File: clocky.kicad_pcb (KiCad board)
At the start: 4 copper layers, 79.9 x 38 mm, 73 parts, among them J1 Bot 50 pin, J2 Bot 40 pin, J3 Top 50 pin, J4 Top 40 pin, J5 Power, J6 JST_PH, J8 Program, Q1 AO3401A, U1 HEF4094B, U10 TMP117xxDRV, U2 HEF4094B, U3 HEF4094B, U4 HEF4094B, U5 HEF4094B, U6 HEF4094B, U7 TPS63060, U8 TPS7A0233PDBV, U9 STM32U031C8Ux, Y1 32768Hz

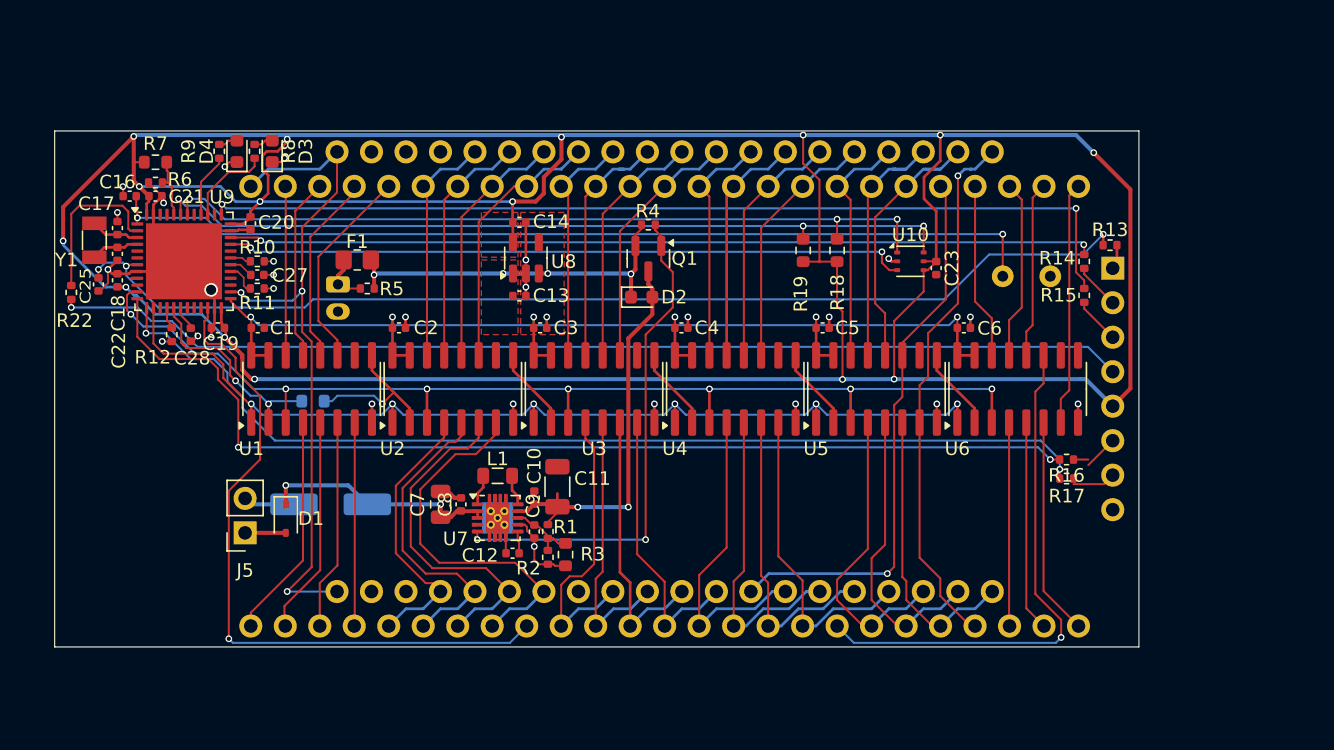
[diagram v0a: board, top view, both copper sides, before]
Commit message: DRC passes.
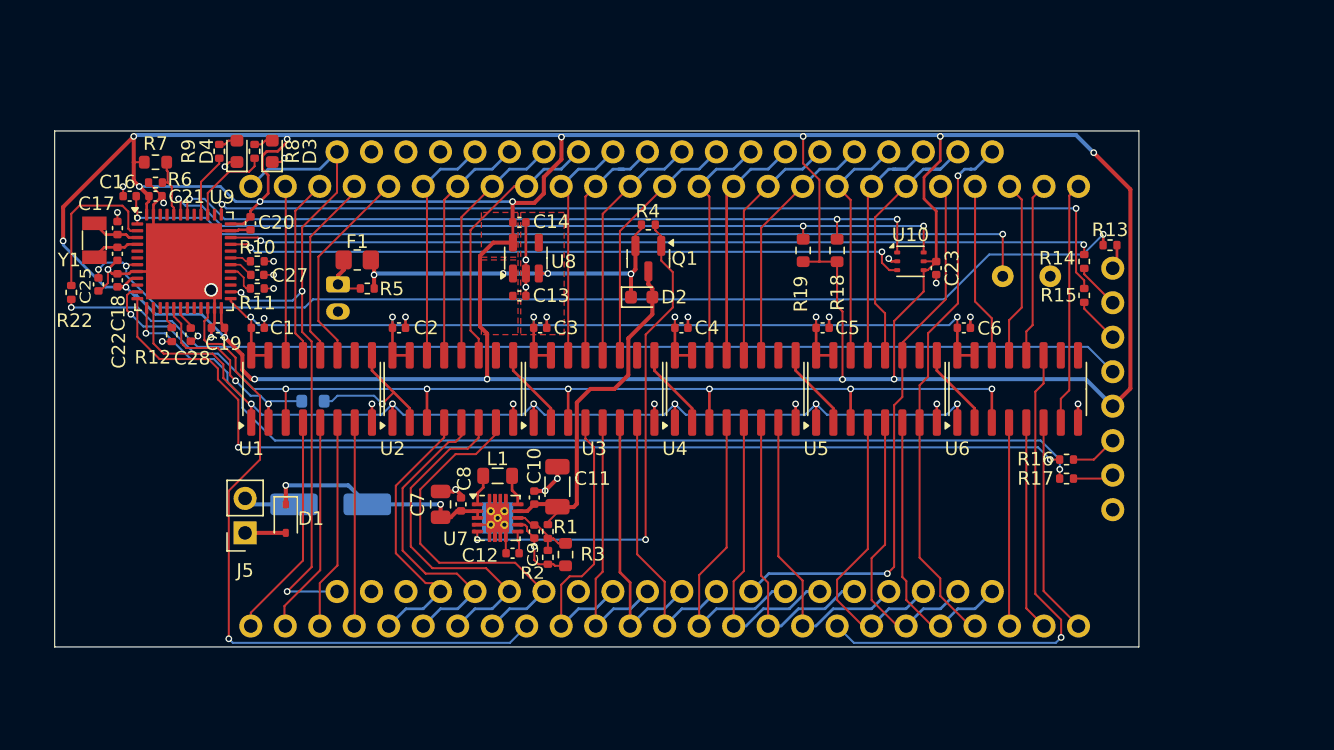
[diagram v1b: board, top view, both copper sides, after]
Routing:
- net +3V3: track 285.6 -> 298.4 mm, vias 15 -> 16
- net GND: track 53.8 -> 58.2 mm, vias 25 -> 30
- net /VBatt: track 29.2 -> 26.0 mm, vias 2 -> 0
- net /Q4D: track 17.5 -> 16.8 mm
- net Net-(U7-FB): track 5.01 -> 4.44 mm
- net /Q2P: track 19.3 -> 19.8 mm
- net /Q2B: track 27.2 -> 26.7 mm

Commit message: Sort the touch pads out a bit.
Zones still need work.
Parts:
- added TP1: TestPoint, Parts:Dummy, F.Cu at (121.2, 90.6)
- added TP2: TestPoint, Parts:Dummy, F.Cu at (121.2, 92.6)
- added TP3: TestPoint, Parts:Dummy, F.Cu at (113.0, 96.5)
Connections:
- R10 pad 1: unconnected-(R10-Pad1) -> /PlusPad
- R11 pad 1: unconnected-(R11-Pad1) -> /MinusPad
- R12 pad 1: unconnected-(R12-Pad1) -> /ExtraPad
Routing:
- net GND: track 58.2 -> 101.6 mm, vias 30 -> 34
- net unconnected-(R11-Pad1): track 27.2 -> 0.00 mm, vias 1 -> 0
- net /MinusPad: track 0.00 -> 27.2 mm, vias 0 -> 1
- net unconnected-(R10-Pad1): track 17.9 -> 0.00 mm, vias 1 -> 0
- net /PlusPad: track 0.00 -> 17.6 mm, vias 0 -> 1
- net unconnected-(R12-Pad1): track 3.40 -> 0.00 mm, vias 1 -> 0
- net /ExtraPad: track 0.00 -> 3.40 mm, vias 0 -> 1

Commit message: Do a round of tidy-up on clocky.
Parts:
- removed R5: 470, Resistor_SMD:R_0402_1005Metric
- added D5: 1N5819WS, Diode_SMD:D_SOD-323, F.Cu at (129.2, 92.4)
- R20: moved to F.Cu
- moved F1 1.85 mm to (129.2, 90.3)
- moved C24 1.00 mm to (126.4, 108.5)
- moved R20 0.91 mm to (124.0, 100.0)
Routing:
- net GND: track 101.6 -> 92.6 mm, vias 34 -> 32
- net +3V3: track 298.4 -> 293.6 mm
- net Net-(D5-A): track 3.32 -> 5.46 mm
- net /Q2F: track 22.5 -> 20.6 mm
- net /Q2A: track 25.0 -> 23.4 mm
- net /Vin: track 17.7 -> 16.3 mm
- net /Q2B: track 26.7 -> 25.4 mm
- net +BATT: track 27.2 -> 25.8 mm
- net /CP: track 82.9 -> 83.9 mm
- net /DAT: track 15.6 -> 16.5 mm
- net /Q3G: track 21.6 -> 20.8 mm
- net /Q2G: track 20.2 -> 19.3 mm
- net /PlusPad: track 17.6 -> 18.4 mm
- net /MinusPad: track 27.2 -> 26.5 mm
- net /SERRX: track 75.3 -> 75.9 mm, vias 2 -> 3
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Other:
- board text added: "3V7"
- board text added: "GND"
- board text added: "Vin"
- board text added: "≡"

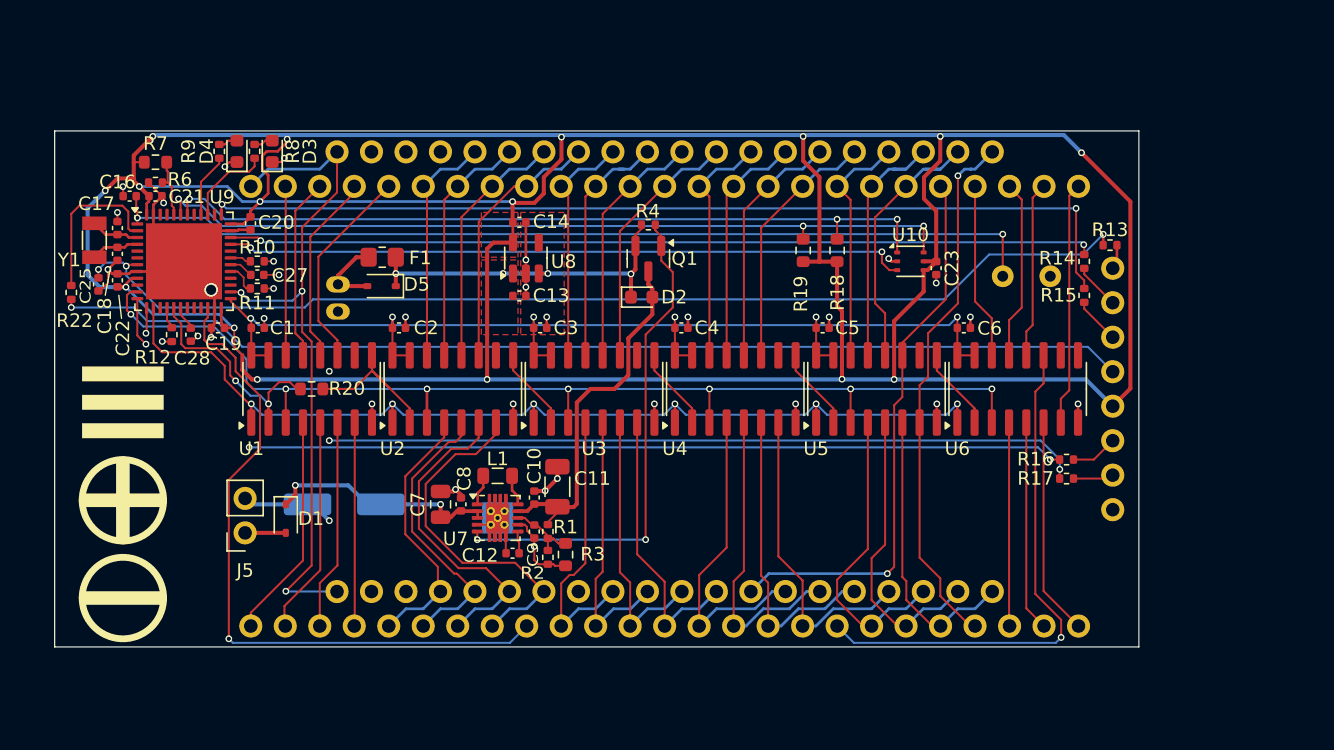
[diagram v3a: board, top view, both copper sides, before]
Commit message: Rotate CPU on clocky.  Tidy up every where.
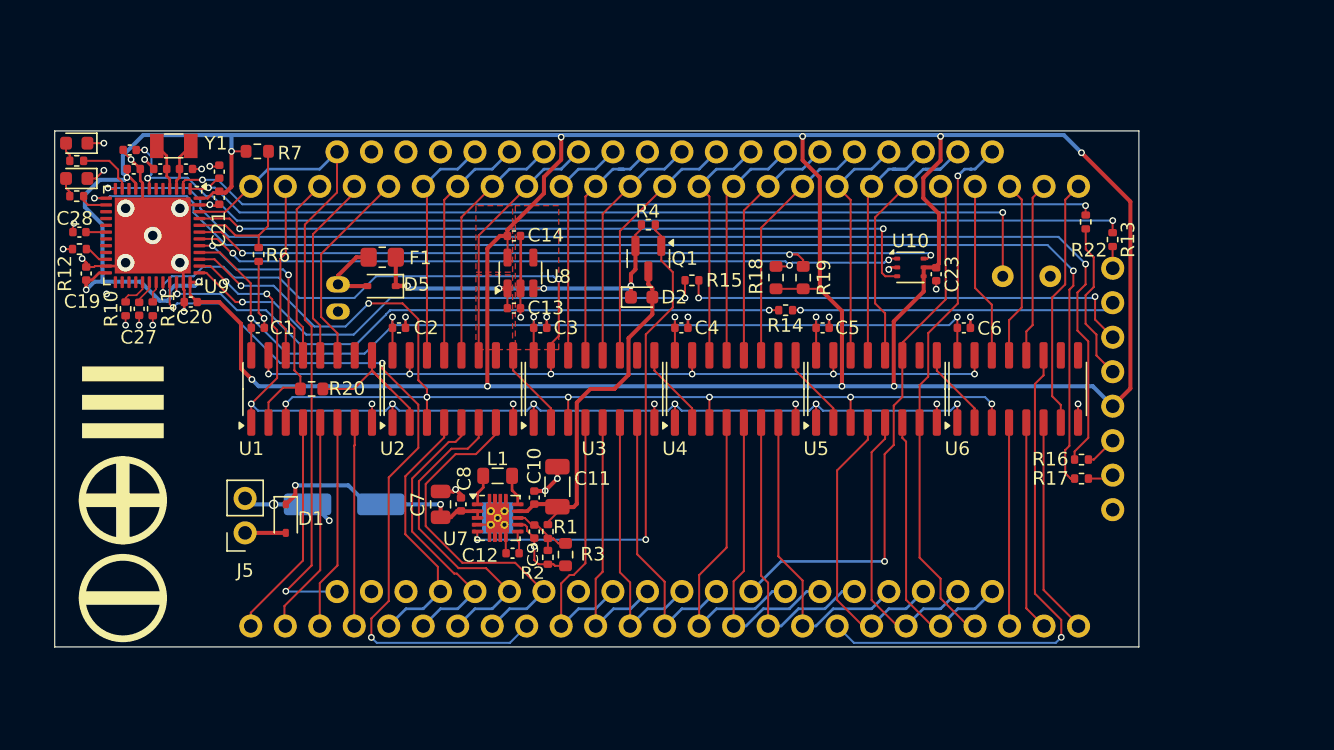
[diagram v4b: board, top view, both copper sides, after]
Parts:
- moved R22 74.9 mm to (181.0, 87.7)
- moved R15 28.9 mm to (152.0, 92.0), turned to 180 degrees
- moved R14 22.3 mm to (158.9, 94.2), turned to 180 degrees
- moved D3 14.4 mm to (106.7, 81.9), turned to 180 degrees
- moved R8 13.1 mm to (106.7, 83.2), turned to 180 degrees
- moved D4 12.0 mm to (106.7, 84.5), turned to 180 degrees
- moved TP1 11.9 mm to (110.3, 95.3), turned to -90 degrees
- moved C28 11.1 mm to (106.9, 88.5), turned to 180 degrees
- moved R9 11.0 mm to (106.7, 85.8), turned to 180 degrees
- moved C19 10.5 mm to (107.4, 91.5), turned to 90 degrees
- moved R10 10.3 mm to (110.3, 94.1), turned to 90 degrees
- moved C25 10.2 mm to (110.6, 82.4), turned to 180 degrees
- moved TP3 9.98 mm to (105.7, 89.7), turned to -90 degrees
- moved TP2 9.30 mm to (112.3, 95.3), turned to -90 degrees
- moved R12 9.27 mm to (106.9, 89.7), turned to 0 degrees
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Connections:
- U1 pad 15: /DPWR -> /OE
- U2 pad 15: /DPWR -> /OE
- U3 pad 15: /DPWR -> /OE
- U4 pad 15: /DPWR -> /OE
- U5 pad 15: /DPWR -> /OE
- U6 pad 15: /DPWR -> /OE
- U9 pad 11: /CP -> /Green
- U9 pad 14: /STR -> /Red
- U9 pad 16: /Extra -> unconnected-(U9-PA6-Pad16)
- U9 pad 17: /DAT -> unconnected-(U9-PA7-Pad17)
- U9 pad 22: /COL1 -> /Extra
- U9 pad 25: /DPWR -> unconnected-(U9-PB12-Pad25)
- U9 pad 26: /COM -> unconnected-(U9-PB13-Pad26)
- U9 pad 29: /Minus -> /Plus
- U9 pad 31: /Plus -> /Minus
- U9 pad 32: unconnected-(U9-PA11-Pad32) -> /OE
- U9 pad 33: /Alert -> /COL1
- U9 pad 38: unconnected-(U9-PA15-Pad38) -> /STR
- U9 pad 39: /Green -> /CP
- U9 pad 40: /Red -> /DPWR
- U9 pad 41: unconnected-(U9-PB5-Pad41) -> /DAT
- U9 pad 45: unconnected-(U9-PB8-Pad45) -> /Alert
- U9 pad 46: unconnected-(U9-PB9-Pad46) -> /COM
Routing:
- net /OE: track 0.00 -> 98.0 mm, vias 0 -> 8
- net /PRTC: track 79.3 -> 11.8 mm, vias 1 -> 0
- net /RTCOUT: track 11.9 -> 68.5 mm, vias 0 -> 2
- net /PSWC: track 3.44 -> 34.0 mm, vias 0 -> 2
- net /SWCLK: track 70.0 -> 40.1 mm
- net /PSWD: track 3.40 -> 23.8 mm, vias 0 -> 1
- net +3V3: track 293.6 -> 273.8 mm, vias 16 -> 12
- net GND: track 92.6 -> 73.0 mm, vias 32 -> 38
- net /SWDIO: track 63.8 -> 47.8 mm
- net /SERRX: track 75.9 -> 91.7 mm, vias 3 -> 2
- net /SERTX: track 76.9 -> 90.6 mm, vias 3 -> 2
- net /BOOT0: track 4.47 -> 12.0 mm
- net /ExtraPad: track 3.39 -> 10.4 mm
- net /Alert: track 50.3 -> 55.2 mm
- net /PlusPad: track 18.4 -> 23.1 mm
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
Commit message: Tweak power & zones.
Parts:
- added D6: 1N4148, Diode_SMD:D_0603_1608Metric, F.Cu at (178.1, 82.2)
- added R5: 100, Resistor_SMD:R_0603_1608Metric, F.Cu at (174.9, 89.0)
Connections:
- C15 pad 1: /VCap -> Net-(C15-Pad1)
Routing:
- net /ExtraPad: track 10.4 -> 15.9 mm
- net /VCap: track 66.2 -> 69.7 mm
- net /PlusPad: track 23.1 -> 21.1 mm
- net Net-(C15-Pad1): track 0.00 -> 1.83 mm
- net /MinusPad: track 30.4 -> 29.0 mm
- net +3V3: track 273.8 -> 274.6 mm
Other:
- board text added: "TODO - decide on main power connector."

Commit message: Final updates.  Ordered.
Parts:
- added R20: 10k, Resistor_SMD:R_0603_1608Metric, F.Cu at (168.1, 88.2)
- C9: footprint Capacitor_SMD:C_0402_1005Metric -> Capacitor_SMD:C_0603_1608Metric
- Q1: value AO3401A -> SI2301A
- U7: footprint Package_SON:Texas_S-PWSON-N10_ThermalVias -> Package_SON:Texas_S-PWSON-N10
- moved D1 6.29 mm to (128.3, 108.5)
- moved R3 3.20 mm to (144.7, 109.7), turned to 90 degrees
- moved R2 2.51 mm to (140.4, 110.1)
- moved C9 2.41 mm to (142.2, 112.1), turned to 0 degrees
- moved J5 1.60 mm to (120.7, 110.6)
- moved R1 0.66 mm to (141.9, 110.1), turned to 0 degrees
- moved R7 0.61 mm to (119.9, 81.9)
- moved R15 0.50 mm to (152.0, 92.5)
- renumbered R20 to R21
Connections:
- R10 pad 1: /PlusPad -> /MinusPad
- R10 pad 2: /Plus -> /Minus
- R11 pad 1: /MinusPad -> /PlusPad
- R11 pad 2: /Minus -> /Plus
- TP1 pad 1: /PlusPad -> /MinusPad
- TP2 pad 1: /MinusPad -> /PlusPad
- U9 pad 29: /Plus -> /Minus
- U9 pad 31: /Minus -> /Plus
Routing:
- net /PlusPad: track 21.1 -> 29.3 mm
- net /MinusPad: track 29.0 -> 21.0 mm
- net Net-(D1-A): track 3.00 -> 8.65 mm, vias 0 -> 1
- net GND: track 73.0 -> 67.9 mm, vias 38 -> 49
- net /Vin: track 16.3 -> 11.3 mm
- net Net-(U7-FB): track 4.44 -> 7.49 mm
- net /Q3G: track 20.8 -> 22.6 mm
- net +3V3: track 274.6 -> 275.9 mm
- net /Alert: track 55.2 -> 56.4 mm
- net /Q3F: track 20.1 -> 20.9 mm
- net /Plus: track 2.32 -> 1.56 mm
- net /Minus: track 1.56 -> 2.32 mm
- net /VBatt: track 26.0 -> 26.6 mm
- net /BOOT0: track 12.0 -> 12.6 mm
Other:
- board text removed: "TODO - decide on main power connector."

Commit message: Tweaks.  Fabbing.
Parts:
- removed the C12 at (138.8, 112.1)
- removed the C13 at (138.9, 94.0)
- removed C24: 220u, Capacitor_SMD:CP_Elec_6.3x7.7
- removed the C7 at (133.5, 108.5)
- removed D4: Red, LED_SMD:LED_0603_1608Metric
- removed D5: 1N5819WS, Diode_SMD:D_SOD-323
- removed F1: 116mA, Resistor_SMD:R_0805_2012Metric_Pad1.20x1.40mm_HandSolder
- removed Q1: SI2301A, Package_TO_SOT_SMD:SOT-23
- removed the R1 at (141.9, 110.1)
- removed the R3 at (144.7, 109.7)
- removed the R4 at (148.8, 87.9)
- removed the R9 at (106.7, 85.8)
- removed U8: TPS7A0233PDBV, Package_TO_SOT_SMD:SOT-23-5
- added C10: 100u, Capacitor_SMD:C_1206_3216Metric, F.Cu at (128.1, 90.2)
- added C23: 1u, Capacitor_SMD:C_0402_1005Metric, F.Cu at (151.7, 107.5)
- added L2: 22u, Inductor_SMD:L_0805_2012Metric_Pad1.05x1.20mm_HandSolder, F.Cu at (152.2, 106.0)
- added R18: 0R, Resistor_SMD:R_0603_1608Metric, F.Cu at (145.6, 112.9)
- added R19: 0R, Resistor_SMD:R_0603_1608Metric, F.Cu at (142.1, 112.9)
- added R21: 845k, Resistor_SMD:R_0603_1608Metric, F.Cu at (161.1, 110.5)
- added R22: 5M6, Resistor_SMD:R_0603_1608Metric, F.Cu at (157.9, 110.5)
- added R23: 3M3, Resistor_SMD:R_0603_1608Metric, F.Cu at (154.7, 110.5)
- added R24: 6M8, Resistor_SMD:R_0603_1608Metric, F.Cu at (161.1, 112.5)
- added R25: 150k, Resistor_SMD:R_0603_1608Metric, F.Cu at (157.9, 112.5)
- added R26: 2M7, Resistor_SMD:R_0603_1608Metric, F.Cu at (154.7, 112.5)
- added R28: 330k, Resistor_SMD:R_0603_1608Metric, F.Cu at (157.9, 108.5)
- added R29: 3M6, Resistor_SMD:R_0603_1608Metric, F.Cu at (154.7, 108.5)
- added TP4: TestPoint_Probe, Parts:TestPoint, F.Cu at (170.8, 106.3)
- added TP5: TestPoint_Probe, Parts:TestPoint, F.Cu at (147.9, 91.8)
- added TP6: TestPoint_Probe, Parts:TestPoint, F.Cu at (173.4, 106.3)
- added TP7: TestPoint_Probe, Parts:TestPoint, F.Cu at (139.1, 105.7)
- C11: footprint Capacitor_SMD:C_1206_3216Metric -> Capacitor_SMD:C_0805_2012Metric
- C12: renamed from C14; value 10u -> 10n
- C27, C28: value 22n -> 330p
- C7: renamed from C10; value 1u -> 10u; footprint Capacitor_SMD:C_0402_1005Metric -> Capacitor_SMD:C_0603_1608Metric
- C8: value 1u -> 10u; footprint Capacitor_SMD:C_0402_1005Metric -> Capacitor_SMD:C_0603_1608Metric
- C9: value 10p -> 10n; footprint Capacitor_SMD:C_0603_1608Metric -> Capacitor_SMD:C_0402_1005Metric
- D2: value 1N4148 -> 5V1; footprint Diode_SMD:D_0603_1608Metric -> Diode_SMD:D_SOD-323
- L1: value 1u -> 10u; footprint Inductor_SMD:L_0805_2012Metric -> Inductor_SMD:L_0805_2012Metric_Pad1.05x1.20mm_HandSolder
- R27: renamed from R2; value 150k -> 6M8; footprint Resistor_SMD:R_0402_1005Metric -> Resistor_SMD:R_0603_1608Metric
- R7: renamed from R10; value 10k -> 1k
- R8: renamed from R11; value 10k -> 1k
- R9: renamed from R12; value 10k -> 1k
- U7: value TPS63060 -> BQ25570; footprint Package_SON:Texas_S-PWSON-N10 -> Package_DFN_QFN:QFN-20-1EP_3.5x3.5mm_P0.5mm_EP2x2mm
- moved C12 23.2 mm to (146.0, 110.8), turned to 180 degrees
- moved R27 20.8 mm to (161.1, 108.5), turned to 180 degrees
- moved D2 16.3 mm to (142.7, 108.5), turned to -90 degrees
- moved C11 14.0 mm to (156.0, 106.0), turned to 0 degrees
- moved C8 13.6 mm to (148.3, 105.5), turned to 0 degrees
- moved D1 12.4 mm to (140.7, 108.5)
- moved U7 11.6 mm to (149.3, 110.1)
- moved C9 8.54 mm to (148.9, 106.8)
- moved L1 8.24 mm to (145.9, 107.2), turned to 0 degrees
- moved C7 5.07 mm to (145.4, 108.8), turned to 0 degrees
- renumbered C23 to C13, C25 to C14, R13 to R1, R5 to R10, R8 to R11, R21 to R12, R6 to R13, R18 to R14, R19 to R15, R20 to R16, R7 to R17, R14 to R2, R15 to R3, R22 to R4, R16 to R5, R17 to R6
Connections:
- net /Green renamed /White
- C11 pad 1: /VBatt -> +3V3
- C12 pad 1: +3V3 -> Net-(U7-VREF_SAMP)
- C7 pad 1: /VBatt -> /Vin
- C8 pad 1: /Vin -> GND
- C8 pad 2: GND -> /VStor
- C9 pad 2: Net-(U7-FB) -> /VStor
- D2 pad 1: +BATT -> /Vin
- D2 pad 2: /VBatt -> GND
- J6 pad 1: Net-(D5-A) -> GND
- J6 pad 2: GND -> /VBatt
- L1 pad 1: Net-(U7-L2) -> /Vin
- L1 pad 2: Net-(U7-L1) -> Net-(U7-LBOOST)
- R27 pad 1: Net-(U7-FB) -> /VRDIV
- R27 pad 2: GND -> /VOUT_SET
- U7 pad 1: Net-(U7-L1) -> GND
- U7 pad 10: Net-(U7-L2) -> /OK_HYST
- U7 pad 11: GND -> /OK_PROG
- U7 pad 3: /Vin -> /VStor
- U7 pad 4: GND -> Net-(U7-VREF_SAMP)
- U7 pad 5: /PGood -> GND
- U7 pad 7: GND -> /VBAT_OV
- U7 pad 8: Net-(U7-FB) -> /VRDIV
- U7 pad 9: /VBatt -> GND
- U9 pad 14: /Red -> unconnected-(U9-PA4-Pad14)
- U9 pad 25: unconnected-(U9-PB12-Pad25) -> /VBatOK
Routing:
- net /VBatOK: track 0.00 -> 54.7 mm, vias 0 -> 3
- net /PGood: track 37.5 -> 0.00 mm, vias 2 -> 0
- net +BATT: track 29.0 -> 0.00 mm, vias 4 -> 0
- net /VRDIV: track 0.00 -> 19.0 mm
- net +3V3: track 275.9 -> 294.2 mm, vias 12 -> 14
- net /VStor: track 0.00 -> 17.8 mm, vias 0 -> 2
- net /VBatt: track 26.6 -> 44.3 mm, vias 0 -> 1
- net /VBAT_OV: track 0.00 -> 12.8 mm
- net Net-(D1-A): track 8.65 -> 20.8 mm
- net /VOUT_SET: track 0.00 -> 10.5 mm
- net /OK_HYST: track 0.00 -> 10.5 mm
- net /OK_PROG: track 0.00 -> 7.68 mm
- net Net-(U7-FB): track 7.49 -> 0.00 mm
- net /Q2B: track 25.4 -> 17.9 mm
- net /Q2A: track 23.4 -> 17.8 mm
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- removed copper zone on F.Cu, net +3V3
- removed copper zone on F.Cu, net +BATT
- removed copper zone on F.Cu, net GND
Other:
- board text added: "3V3"
- board text added: "RST"
- board text added: "RTC"
- board text added: "RX"
- board text added: "SWC"
- board text added: "SWD"
- board text added: "TX"
- board text added: "VBatt"
